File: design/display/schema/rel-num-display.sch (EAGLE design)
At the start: 1 part, among them IC1 7476N

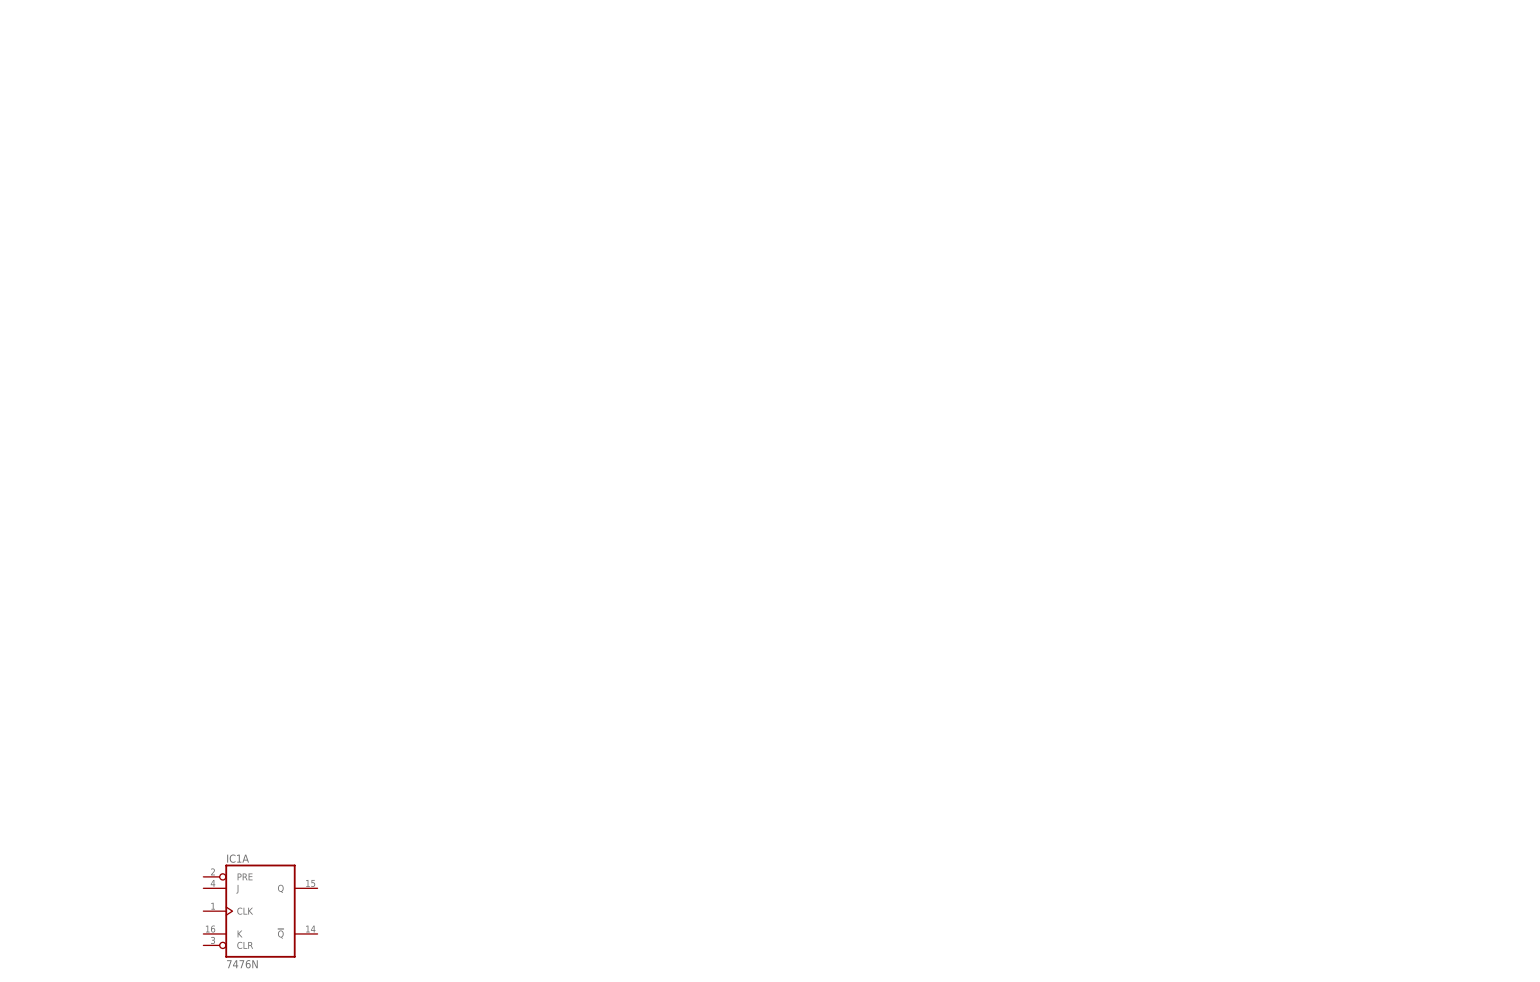
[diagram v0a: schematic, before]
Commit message: Added final fixes and program changes for numerical display
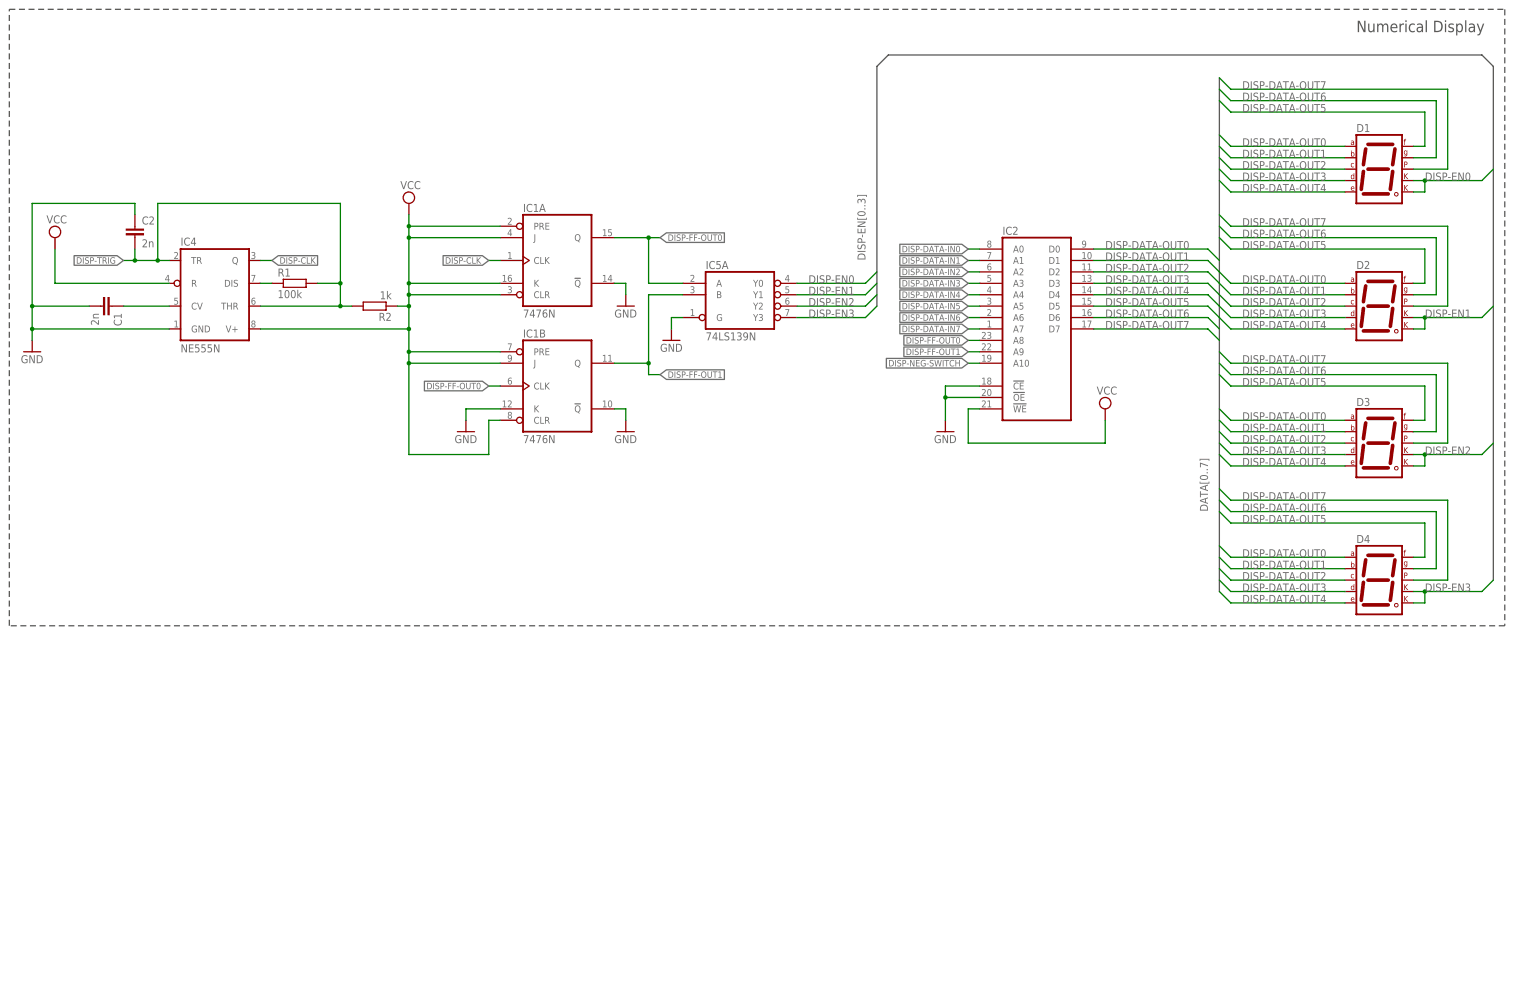
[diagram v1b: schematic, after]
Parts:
- added C1, C2: 2n, resistor:C-EU025-025X050
- added D1, D2, D3, D4: (no value), special:7SEG-CK
- added IC2: (no value), memory:2816
- added IC4: NE555N, linear:NE555N
- added IC5: 74LS139N, 74xx-eu:74LS139N
- added R1: 100k, resistor:R-EU_0204/5
- added R2: 1k, resistor:R-EU_0204/5
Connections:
- new net DISP-CLK: IC1A.CLK, IC4.Q
- new net DISP-DATA-IN0: IC2A.A0
- new net DISP-DATA-IN1: IC2A.A1
- new net DISP-DATA-IN2: IC2A.A2
- new net DISP-DATA-IN3: IC2A.A3
- new net DISP-DATA-IN4: IC2A.A4
- new net DISP-DATA-IN5: IC2A.A5
- new net DISP-DATA-IN6: IC2A.A6
- new net DISP-DATA-IN7: IC2A.A7
- new net DISP-DATA-OUT0: D1.A, D2.A, D3.A, D4.A, IC2A.D0
- new net DISP-DATA-OUT1: D1.B, D2.B, D3.B, D4.B, IC2A.D1
- new net DISP-DATA-OUT2: D1.C, D2.C, D3.C, D4.C, IC2A.D2
- new net DISP-DATA-OUT3: D1.D, D2.D, D3.D, D4.D, IC2A.D3
- new net DISP-DATA-OUT4: D1.E, D2.E, D3.E, D4.E, IC2A.D4
- new net DISP-DATA-OUT5: D1.F, D2.F, D3.F, D4.F, IC2A.D5
- new net DISP-DATA-OUT6: D1.G, D2.G, D3.G, D4.G, IC2A.D6
- new net DISP-DATA-OUT7: D1.DP, D2.DP, D3.DP, D4.DP, IC2A.D7
- new net DISP-EN0: D1.CK1, D1.CK2, IC5A.Y0
- new net DISP-EN1: D2.CK1, D2.CK2, IC5A.Y1
- new net DISP-EN2: D3.CK1, D3.CK2, IC5A.Y2
- new net DISP-EN3: D4.CK1, D4.CK2, IC5A.Y3
- new net DISP-FF-OUT0: IC1A.Q, IC1B.CLK, IC2A.A8, IC5A.A
- new net DISP-FF-OUT1: IC1B.Q, IC2A.A9, IC5A.B
- new net DISP-NEG-SWITCH: IC2A.A10
- new net DISP-TRIG: C2.2, IC4.THR, IC4.TR, R1.2, R2.2
- new net GND: C1.2, C2.1, IC1A.!Q, IC1B.!Q, IC1B.K, IC2A.!CE, IC2A.!OE, IC4.GND, IC5A.G
- new net N$1: IC4.DIS, R1.1
- new net N$6: C1.1, IC4.CV
- new net VCC: IC1A.CLR, IC1A.J, IC1A.K, IC1A.PRE, IC1B.CLR, IC1B.J, IC1B.PRE, IC2A.!WE, IC4.R, IC4.V+, R2.1
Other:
- note added: "Numerical Display"
- moved on the sheet: IC1A

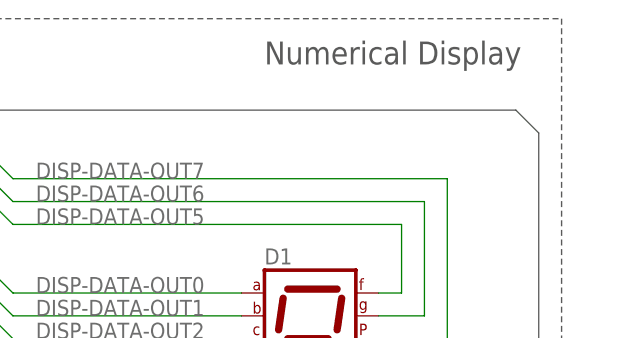
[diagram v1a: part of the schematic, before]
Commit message: Added initial version of control unit schema
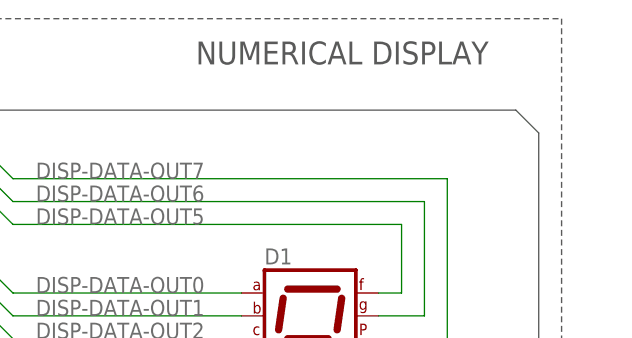
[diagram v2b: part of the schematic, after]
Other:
- note added: "NUMERICAL DISPLAY"
- note removed: "Numerical Display"
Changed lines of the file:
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@@
 <?xml version="1.0" encoding="utf-8"?>
 <!DOCTYPE eagle SYSTEM "eagle.dtd">
-<eagle version="9.1.3">
+<eagle version="9.6.2">
 <drawing>
 <settings>
@@
 <wire x1="-48.26" y1="139.7" x2="-48.26" y2="276.86" width="0.1524" layer="97" style="shortdash"/>
 <wire x1="-48.26" y1="276.86" x2="284.48" y2="276.86" width="0.1524" layer="97" style="shortdash"/>
-<text x="251.46" y="271.78" size="2.54" layer="97">Numerical Display</text>
+<text x="243.84" y="271.78" size="2.54" layer="97">NUMERICAL DISPLAY</text>
 </plain>
 <instances>

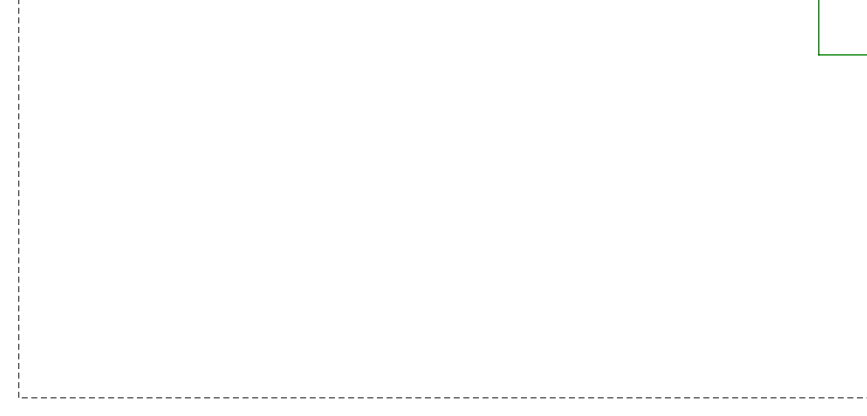
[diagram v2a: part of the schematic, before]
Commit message: Added version number to each schema
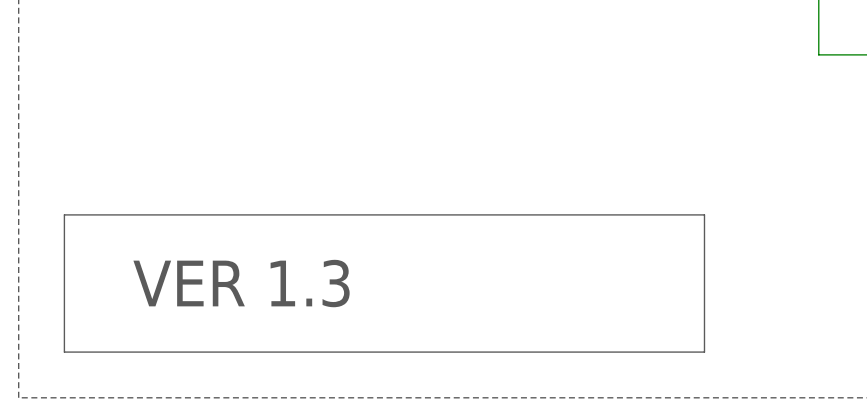
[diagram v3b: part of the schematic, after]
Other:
- note added: "VER 1.3"
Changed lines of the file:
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@@
 <wire x1="-48.26" y1="276.86" x2="284.48" y2="276.86" width="0.1524" layer="97" style="shortdash"/>
 <text x="243.84" y="271.78" size="2.54" layer="97">NUMERICAL DISPLAY</text>
+<wire x1="-43.18" y1="160.02" x2="-43.18" y2="144.78" width="0.1524" layer="97"/>
+<wire x1="-43.18" y1="144.78" x2="27.94" y2="144.78" width="0.1524" layer="97"/>
+<wire x1="27.94" y1="144.78" x2="27.94" y2="160.02" width="0.1524" layer="97"/>
+<wire x1="27.94" y1="160.02" x2="-43.18" y2="160.02" width="0.1524" layer="97"/>
+<text x="-35.56" y="149.86" size="5.08" layer="97">VER 1.3</text>
 </plain>
 <instances>
